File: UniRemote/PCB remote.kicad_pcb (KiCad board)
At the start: 2 copper layers, 44.5 x 140 mm, 20 parts, among them J1 Conn_01x01, J2 Conn_01x01, J3 02_Socket, J4 Conn_01x02_Socket, Q1 PMV28XPEAR, Q2 BSS138, SW1 GREEN, SW2 RED, U1 RFM69HW, U2 SSD1306, U3 Joystick, U4 HW373

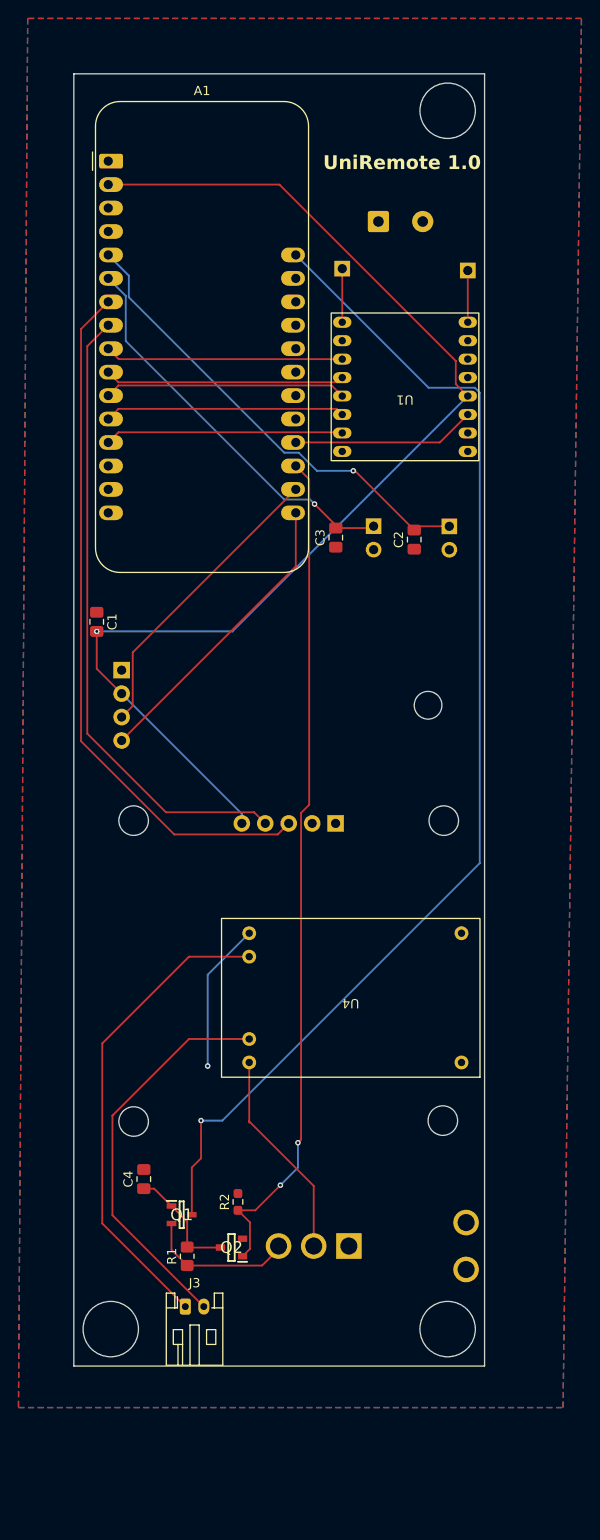
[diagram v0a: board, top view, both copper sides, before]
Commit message: Har lavet begge pcber om. Remote har ændret struktur for mere håndholdt design og ekstra knapper plus LEDer. roboside har fået ny relay og LEDer
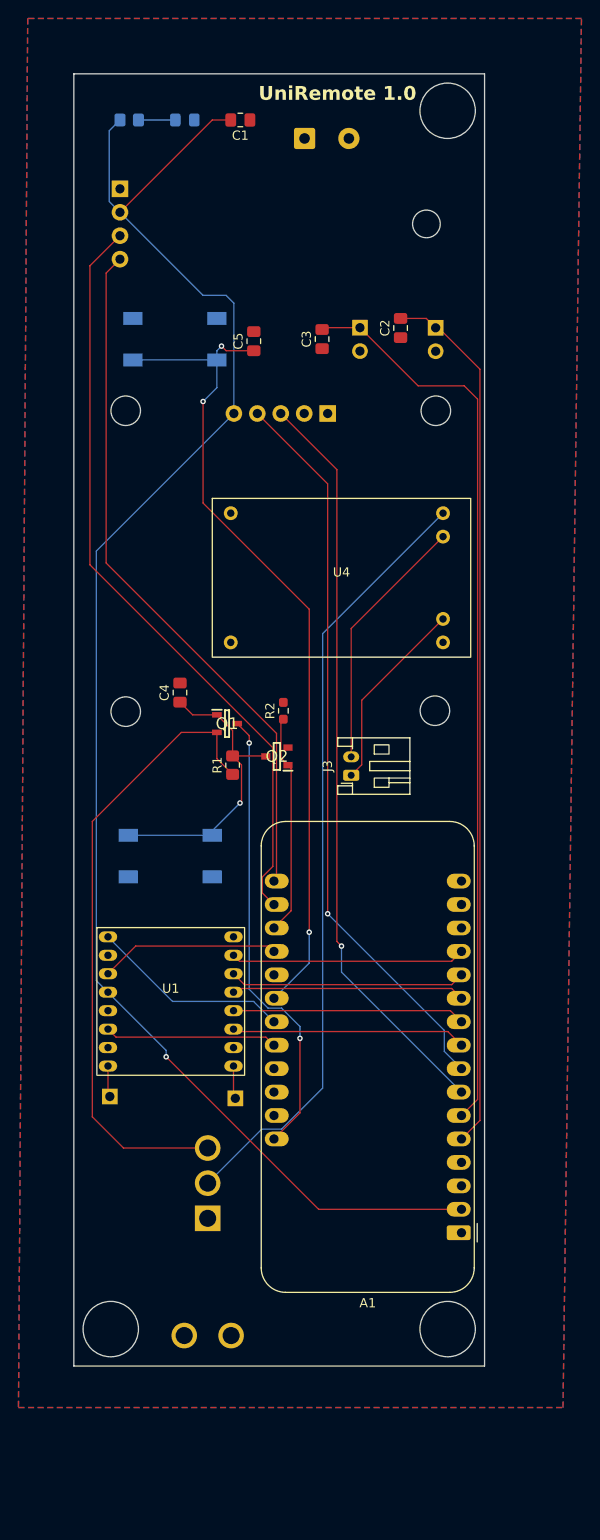
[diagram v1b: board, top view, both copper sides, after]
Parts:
- added C5: 100nF, Capacitor_SMD:C_0805_2012Metric_Pad1.18x1.45mm_HandSolder, F.Cu at (49.5, 59.0)
- added D1: LED, LED_SMD:LED_0805_2012Metric_Pad1.15x1.40mm_HandSolder, B.Cu at (42.0, 35.0)
- added R3: 330, Resistor_SMD:R_0805_2012Metric_Pad1.20x1.40mm_HandSolder, B.Cu at (36.0, 35.0)
- added S2: TL3301TF160QG, Remote-footprints:TL3301TF160QG, B.Cu at (40.5, 114.8)
- added S3: TL3301TF160QG, Remote-footprints:TL3301TF160QG, B.Cu at (41.0, 58.8)
- moved A1 122.2 mm to (72.0, 155.6), turned to 180 degrees
- moved J1 97.5 mm to (33.9, 140.8), turned to 180 degrees
- moved J2 90.6 mm to (47.5, 141.0), turned to 180 degrees
- moved U1 71.3 mm to (40.5, 130.5), turned to 0 degrees
- moved J3 60.3 mm to (60.0, 106.0), turned to 90 degrees
- moved C1 56.6 mm to (48.0, 35.0), turned to 180 degrees
- moved Q1 53.4 mm to (46.6, 100.4)
- moved R1 53.4 mm to (47.2, 104.9)
- moved Q2 53.4 mm to (52.0, 104.0)
- moved R2 53.4 mm to (52.7, 99.0)
- moved C4 52.9 mm to (41.5, 97.0)
- moved U2 52.2 mm to (52.5, 46.3)
- moved U4 45.7 mm to (59.0, 84.5), turned to 0 degrees
- moved U3 44.4 mm to (52.4, 82.8)
- moved C2 23.0 mm to (65.4, 57.5)
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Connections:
- A1 pad 22: unconnected-(A1-D10-Pad22) -> Button
- A1 pad 23: unconnected-(A1-D11-Pad23) -> DIO2
- A1 pad 24: unconnected-(A1-D12-Pad24) -> DIO3
- S1 pad 4: unconnected-(S1-MH1-Pad4) -> GND
- S1 pad 5: unconnected-(S1-MH2-Pad5) -> GND
- U1 pad 1: unconnected-(U1-DIO2-Pad1) -> DIO2
- U1 pad 6: unconnected-(U1-DIO3-Pad6) -> DIO3
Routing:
- net Button: track 0.00 -> 90.6 mm, vias 0 -> 3
- net +BATT: track 129.5 -> 49.8 mm, vias 1 -> 2
- net PWRControl: track 91.4 -> 24.0 mm, vias 2 -> 0
- net Net-(S1-COM): track 22.9 -> 84.4 mm
- net Net-(A1-A1): track 43.1 -> 98.5 mm, vias 1 -> 0
- net Net-(Q1-S): track 16.4 -> 68.7 mm
- net Net-(A1-SCL/D21): track 32.5 -> 83.0 mm
- net +3.3V: track 128.0 -> 173.3 mm
- net Net-(A1-DAC0/A0): track 50.8 -> 95.1 mm, vias 1 -> 0
- net Net-(A1-SDA/D20): track 32.5 -> 75.8 mm
- net Net-(J3-Pin_1): track 52.1 -> 21.1 mm
- net DIO2: track 0.00 -> 21.8 mm
- net Net-(Q1-G): track 12.6 -> 32.8 mm, vias 0 -> 1
- net DIO3: track 0.00 -> 18.7 mm
- net GND: track 16.3 -> 0.00 mm, vias 1 -> 0
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
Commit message: pcb
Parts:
- moved C2 1.00 mm to (65.5, 58.5)
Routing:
- net Net-(S1-COM): track 84.4 -> 101.0 mm, vias 0 -> 1
- net Button: track 90.6 -> 94.9 mm
- net +BATT: track 49.8 -> 53.9 mm, vias 2 -> 1
- net PWRControl: track 24.0 -> 26.7 mm, vias 0 -> 2
- net Net-(A1-SDA/D20): track 75.8 -> 77.4 mm
- net +3.3V: track 173.3 -> 172.0 mm, vias 1 -> 2
- net Net-(A1-A5): track 25.2 -> 26.2 mm
- net Net-(A1-A4): track 25.4 -> 26.4 mm
- net Net-(A1-A2): track 81.6 -> 82.5 mm, vias 1 -> 0
- net Net-(A1-SCK/D24): track 25.3 -> 26.0 mm
- net Net-(Q1-S): vias 0 -> 2

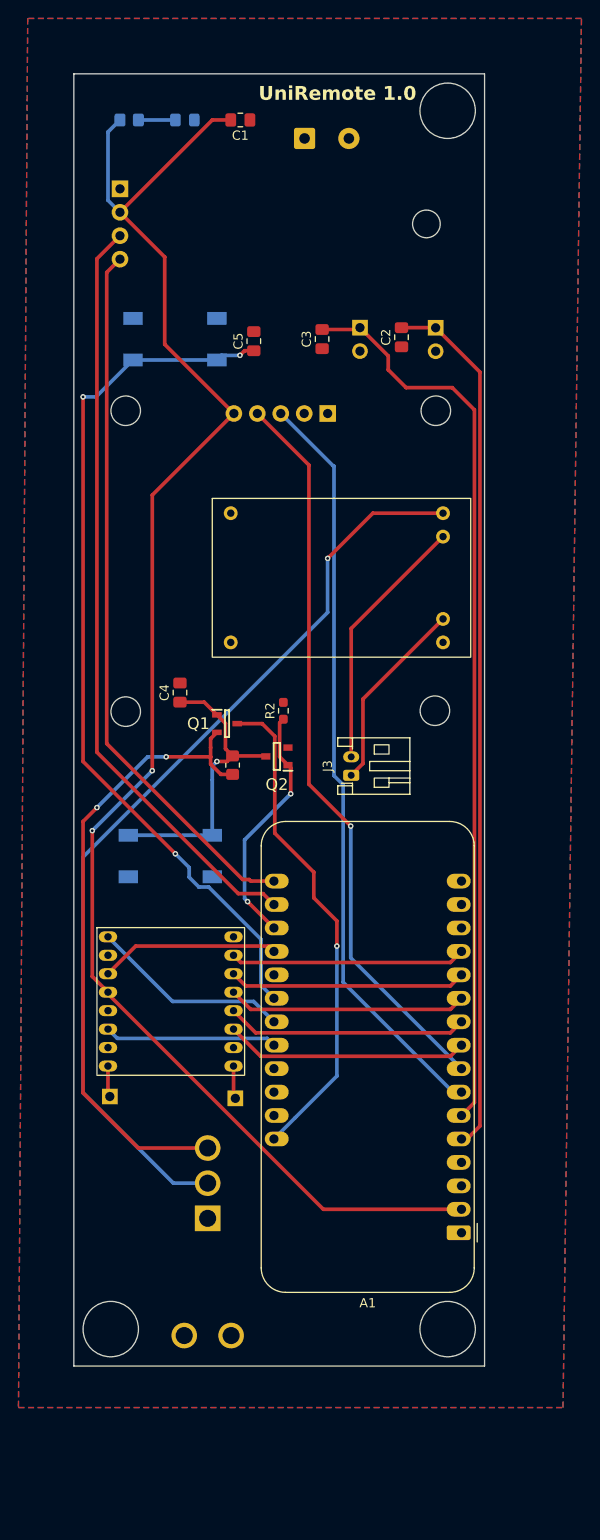
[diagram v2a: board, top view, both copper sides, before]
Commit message: Add test scripts, PCB design files, and appendix code listings
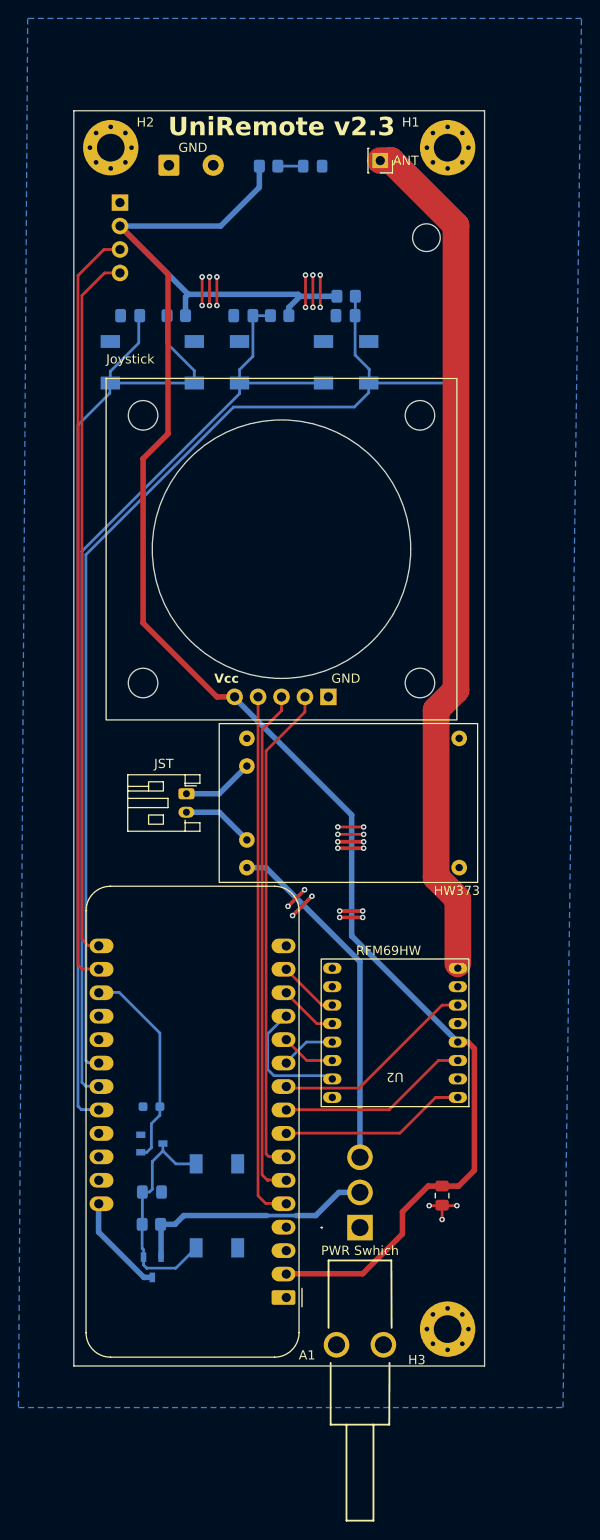
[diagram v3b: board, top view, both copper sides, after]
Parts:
- removed J1, J2: Conn_01x01, Connector_PinSocket_2.54mm:PinSocket_1x01_P2.54mm_Vertical
- removed J3: 02_Socket, Connector_JST:JST_PH_S2B-PH-K_1x02_P2.00mm_Horizontal
- removed J4: Conn_01x02_Socket, Connector_Wire:SolderWire-0.5sqmm_1x02_P4.8mm_D0.9mm_OD2.3mm
- removed SW1: GREEN, Connector_PinSocket_2.54mm:PinSocket_1x02_P2.54mm_Vertical
- removed SW2: RED, Connector_PinSocket_2.54mm:PinSocket_1x02_P2.54mm_Vertical
- removed U1: RFM69HW, Remote-footprints:RFM69HCW(homemade)
- removed U4: HW373, Remote-footprints:HW373
- added ANT: Conn_01x01, Connector_PinSocket_2.54mm:PinSocket_1x01_P2.54mm_Vertical, F.Cu at (63.2, 39.4)
- added GND: Conn_01x02_Socket, Connector_Wire:SolderWire-0.5sqmm_1x02_P4.8mm_D0.9mm_OD2.3mm, F.Cu at (40.3, 39.9)
- added H1: MountingHole_Pad, MountingHole:MountingHole_3mm_Pad_Via, F.Cu at (70.5, 38.0)
- added H2: MountingHole_Pad, MountingHole:MountingHole_3mm_Pad_Via, F.Cu at (34.0, 38.0)
- added H3: MountingHole_Pad, MountingHole:MountingHole_3mm_Pad_Via, F.Cu at (70.5, 166.0)
- added HW373: HW373, Remote-footprints:HW373, F.Cu at (59.8, 109.1)
- added JST: 02_Socket, Connector_JST:JST_PH_S2B-PH-K_1x02_P2.00mm_Horizontal, F.Cu at (42.2, 108.0)
- added PWR Swhich: 100SP1T1B1M7QEH, Remote-footprints:100SP1T1B1M7QEH(redSwitch), F.Cu at (61.0, 155.0)
- added R4: 10k, Resistor_SMD:R_0805_2012Metric_Pad1.20x1.40mm_HandSolder, B.Cu at (59.5, 54.1)
- added R5: 10k, Resistor_SMD:R_0805_2012Metric_Pad1.20x1.40mm_HandSolder, B.Cu at (52.3, 56.2)
- added R6: 10k, Resistor_SMD:R_0805_2012Metric_Pad1.20x1.40mm_HandSolder, B.Cu at (41.1, 56.2)
- added S5: TL3301TF160QG, Remote-footprints:TL3301TF160QG, B.Cu at (45.5, 152.7)
- added SSD1306: SSD1306, Remote-footprints:SSD1306(128x32), B.Cu at (52.5, 47.8)
- C2, C3, R2: moved to B.Cu
- C4: value 10uF -> 100nF; moved to B.Cu
- C5: value 100nF -> 10uF; moved to B.Cu
- Q1: value PMV28XPEAR -> BSS138; footprint Remote-footprints:Pmos -> Remote-footprints:nmos; moved to B.Cu
- Q2: value BSS138 -> PMV28XPEAR; footprint Remote-footprints:nmos -> Remote-footprints:Pmos; moved to B.Cu
- R1: value 220k -> 280; moved to B.Cu
- R3: value 330 -> 220k
- S1: value 100SP1T1B1M7QEH -> TL3301TF160QG; footprint Remote-footprints:100SP1T1B1M7QEH(redSwitch) -> Remote-footprints:TL3301TF160QG
- U2: value SSD1306 -> RFM69HW; footprint Remote-footprints:SSD1306(128x32) -> Remote-footprints:RFM69HCW(homemade); moved to F.Cu
- U3: moved to F.Cu
- moved R3 119.7 mm to (38.4, 154.7), turned to 180 degrees
- moved C1 118.6 mm to (69.9, 151.5), turned to 90 degrees
- moved S1 95.3 mm to (66.5, 61.2)
- moved C5 92.8 mm to (38.5, 151.2), turned to 0 degrees
- moved U2 88.5 mm to (64.8, 133.9), turned to 180 degrees
- moved R1 65.0 mm to (51.1, 40.0), turned to 0 degrees
- moved Q2 57.0 mm to (38.5, 159.3), turned to -90 degrees
- moved S2 54.8 mm to (52.5, 61.2), turned to 90 degrees
- moved Q1 46.2 mm to (38.5, 145.9)
- moved R2 45.2 mm to (38.4, 141.9), turned to 180 degrees
- moved C4 41.2 mm to (36.1, 56.2), turned to 180 degrees
- moved A1 20.2 mm to (53.0, 162.6)
- moved D1 14.7 mm to (55.9, 40.0)
- moved C3 8.91 mm to (48.4, 56.2), turned to 180 degrees
- moved C2 6.50 mm to (59.4, 56.2), turned to 180 degrees
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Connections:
- A1 pad 10: Net-(A1-A5) -> /R-A5-DO3
- A1 pad 11: Net-(A1-SCK/D24) -> /R-D24-SCK
- A1 pad 12: Net-(A1-MOSI/D23) -> /R-D23-MOSI
- A1 pad 13: Net-(A1-MISO/D22) -> /R-D22-MISO
- A1 pad 14: unconnected-(A1-RX/D0-Pad14) -> /R-D0-NSS
- A1 pad 15: unconnected-(A1-TX/D1-Pad15) -> /R-D1-RT
- A1 pad 17: Net-(A1-SDA/D20) -> /SDA
- A1 pad 18: Net-(A1-SCL/D21) -> /SCL
- A1 pad 19: PWRControl -> PWRC
- A1 pad 20: Net-(A1-D6) -> unconnected-(A1-D6-Pad20)
- A1 pad 22: Button -> /B-D10-S1
- A1 pad 23: DIO2 -> /B-D11-S2
- A1 pad 24: DIO3 -> /B-D12-S3
- A1 pad 5: Net-(A1-DAC0/A0) -> /J-A2-Xout
- A1 pad 6: Net-(A1-A1) -> /J-A1-Yout
- A1 pad 7: Net-(A1-A2) -> /J-A0-Sel
- A1 pad 8: Net-(A1-A3) -> /R-A3-D02
- A1 pad 9: Net-(A1-A4) -> /R-A4-DO0
- C2 pad 1: GND -> /B-D10-S1
- C2 pad 2: Net-(A1-DAC0/A0) -> GND
- C3 pad 1: GND -> /B-D11-S2
- C3 pad 2: Net-(A1-A1) -> GND
- C4 pad 1: Net-(Q1-G) -> /B-D12-S3
- C5 pad 1: Button -> Net-(Q1-D)
- Q1 pad 1: Net-(Q1-G) -> PWRC
- Q1 pad 2: Net-(Q1-S) -> GND
- Q1 pad 3: +BATT -> Net-(Q1-D)
- Q2 pad 1: PWRControl -> Net-(Q1-D)
- Q2 pad 2: GND -> /P-S4-BAT
- Q2 pad 3: Net-(Q1-G) -> +BATT
- R1 pad 1: Net-(Q1-S) -> +3.3V
- R1 pad 2: Net-(Q1-G) -> Net-(D1-A)
- R2 pad 1: PWRControl -> PWRC
- R3 pad 1: +3.3V -> /P-S4-BAT
- R3 pad 2: Net-(D1-A) -> Net-(Q1-D)
- S1 pad 1: unconnected-(S1-NC-Pad1) -> /B-D10-S1
- S1 pad 2: Net-(S1-COM) -> /B-D10-S1
- S1 pad 3: Net-(Q1-S) -> GND
- S2 pad 1: Net-(Q1-G) -> /B-D11-S2
- S2 pad 2: Net-(Q1-G) -> /B-D11-S2
- S3 pad 1: Button -> /B-D12-S3
- S3 pad 2: Button -> /B-D12-S3
- U2 pad 1: GND -> /R-A3-D02
- U2 pad 2: +3.3V -> unconnected-(U2-DIO1-Pad2)
- U2 pad 3: Net-(A1-SCL/D21) -> /R-A4-DO0
- U2 pad 4: Net-(A1-SDA/D20) -> +3.3V
- U3 pad 2: unconnected-(U3-Sel-Pad2) -> /J-A0-Sel
- U3 pad 3: Net-(A1-A2) -> /J-A1-Yout
- U3 pad 4: Net-(A1-A3) -> /J-A2-Xout
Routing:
- net /B-D10-S1: track 0.00 -> 114.4 mm
- net /B-D12-S3: track 0.00 -> 108.3 mm
- net /B-D11-S2: track 0.00 -> 104.1 mm
- net Net-(S1-COM): track 101.0 -> 0.00 mm, vias 1 -> 0
- net Net-(A1-A1): track 98.2 -> 0.00 mm
- net Button: track 94.9 -> 0.00 mm, vias 3 -> 0
- net Net-(A1-DAC0/A0): track 94.8 -> 0.00 mm
- net Net-(J2-Pin_1): track 3.58 -> 93.5 mm
- net Net-(A1-SCL/D21): track 83.0 -> 0.00 mm
- net /SCL: track 0.00 -> 82.8 mm
- net Net-(A1-A2): track 82.5 -> 0.00 mm
- net Net-(A1-A3): track 80.1 -> 0.00 mm, vias 1 -> 0
- net Net-(A1-SDA/D20): track 77.4 -> 0.00 mm
- net /SDA: track 0.00 -> 77.0 mm
- net Net-(Q1-S): track 68.7 -> 0.00 mm, vias 2 -> 0
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- removed copper zone on F.Cu, net GND
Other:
- board size 44.5 x 140 mm -> 44.5 x 136 mm
- board text added: "ANT"
- board text added: "PowerLED"
- board text added: "UniRemote v2.3"
- board text removed: "UniRemote 1.0"
